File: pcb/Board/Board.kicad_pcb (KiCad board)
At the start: 2 copper layers, 132.1 x 73.3 mm, 69 parts, among them J1 Conn_01x04_Female, J2 TRRS_SJ1-42514, J3 Conn_01x12_Female, K00 KEYSW, K01 KEYSW, K02 KEYSW, K03 KEYSW, K04 KEYSW, K05 KEYSW, K10 KEYSW, K11 KEYSW, K12 KEYSW, K13 KEYSW, K14 KEYSW, K15 KEYSW, K20 KEYSW, K21 KEYSW, K22 KEYSW, K23 KEYSW, K24 KEYSW, K25 KEYSW, K26 KEYSW, K30 KEYSW, K31 KEYSW, K32 KEYSW, K33 KEYSW, K34 KEYSW, K35 KEYSW, K36 KEYSW, U2 PI6ULS5V9511AWEX_I2C_HotSwap, U3 MCP23017_SO

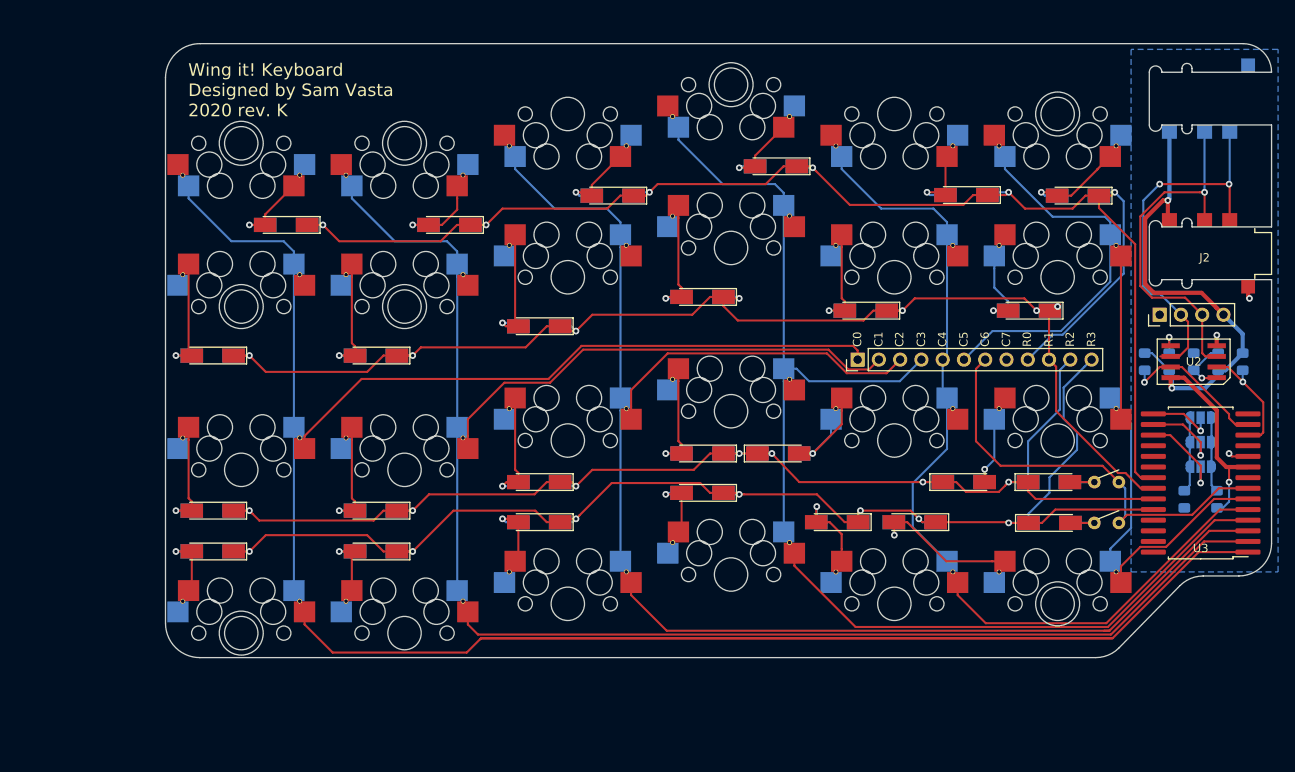
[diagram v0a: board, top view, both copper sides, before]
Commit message: Changed i/o expander to ssop package
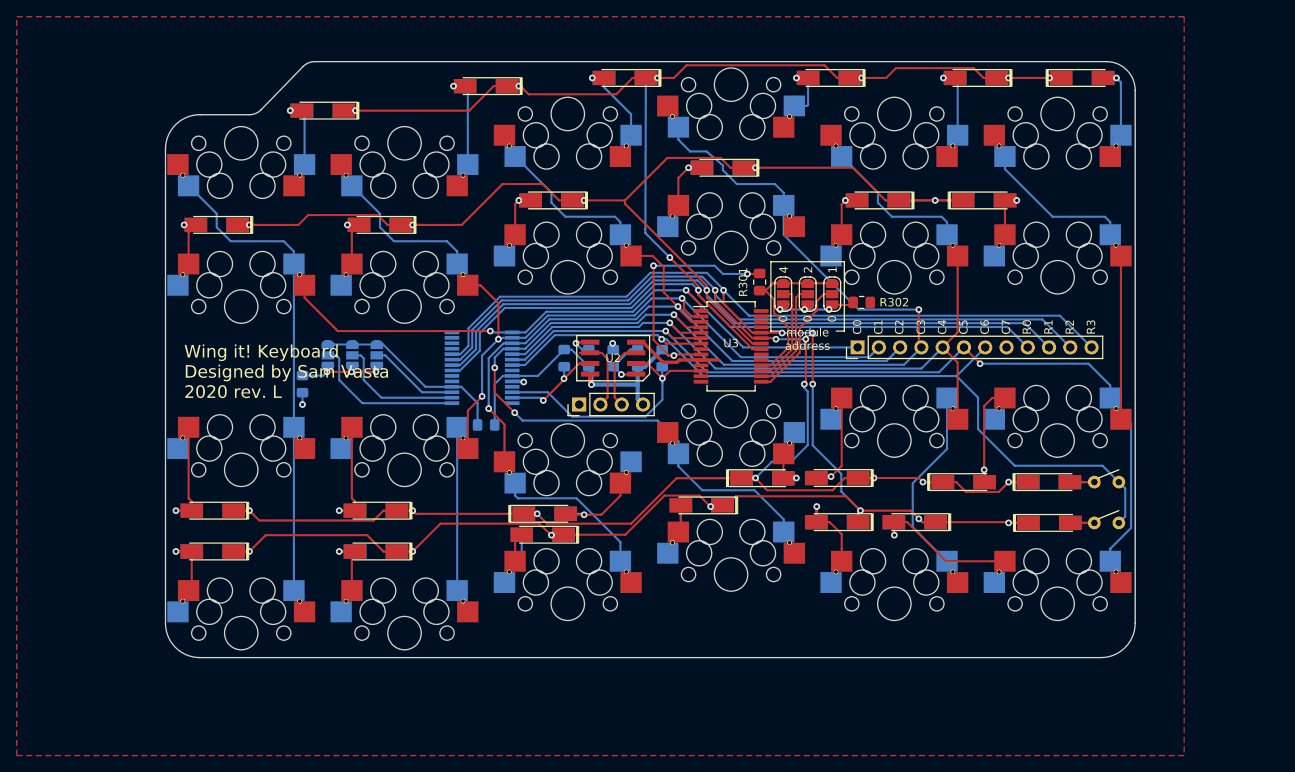
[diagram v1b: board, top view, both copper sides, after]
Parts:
- removed the G*** at (213.3, 48.9)
- removed J2 (x2): TRRS_SJ1-42514, SVastaCustomParts:3.5mm_Cut_out
- removed the U3 at (321.5, 95.3)
- added G***: LOGO, SVastaCustomParts:wing_it_small, B.Cu at (265.4, 111.3)
- added JP0: SolderJumper_3_Open, Jumper:SolderJumper-3_P1.3mm_Open_RoundedPad1.0x1.5mm, F.Cu at (277.5, 72.8)
- added JP1: SolderJumper_3_Open, Jumper:SolderJumper-3_P1.3mm_Open_RoundedPad1.0x1.5mm, F.Cu at (274.6, 72.8)
- added JP2: SolderJumper_3_Open, Jumper:SolderJumper-3_P1.3mm_Open_RoundedPad1.0x1.5mm, F.Cu at (271.6, 72.8)
- added R301: 10K, Resistor_SMD:R_0805_2012Metric_Pad1.15x1.40mm_HandSolder, F.Cu at (268.8, 71.3)
- added R302: 10K, Resistor_SMD:R_0805_2012Metric_Pad1.15x1.40mm_HandSolder, F.Cu at (281.0, 73.8)
- added U3: MCP23017_SO, Package_SO:SSOP-28_5.3x10.2mm_P0.65mm, B.Cu at (235.7, 81.6)
- added U3: MCP23017_SO, Package_SO:SSOP-28_5.3x10.2mm_P0.65mm, F.Cu at (265.4, 79.0)
- moved R302 106.2 mm to (214.2, 83.5)
- moved JP0 104.5 mm to (217.3, 80.1), turned to 270 degrees
- moved JP1 101.8 mm to (220.2, 80.1), turned to 270 degrees
- moved JP2 99.3 mm to (223.1, 80.1), turned to 270 degrees
- moved R301 87.7 mm to (236.2, 88.4), turned to 0 degrees
- moved J1 70.1 mm to (247.3, 86.0)
- moved R201 69.3 mm to (254.3, 80.4)
- moved R203 69.3 mm to (245.5, 80.4)
- moved C201 69.3 mm to (251.3, 80.4)
- moved R202 69.3 mm to (257.2, 80.4)
- moved R204 69.3 mm to (248.4, 80.4)
- moved U2 69.3 mm to (251.3, 80.4)
- moved D01 17.1 mm to (236.2, 47.9)
- moved D13 15.6 mm to (264.4, 57.7)
- moved D10 15.6 mm to (204.0, 64.5)
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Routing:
- net /SwitchMatrix/Col0: track 339.5 -> 147.6 mm, vias 0 -> 2
- net /SwitchMatrix/Col1: track 226.8 -> 128.1 mm, vias 0 -> 3
- net /SwitchMatrix/Row2: track 151.0 -> 232.6 mm, vias 7 -> 11
- net /SwitchMatrix/Row3: track 159.2 -> 240.0 mm, vias 7 -> 11
- net /SwitchMatrix/Row1: track 147.1 -> 215.2 mm, vias 7 -> 6
- net /SwitchMatrix/Col2: track 191.1 -> 130.7 mm, vias 0 -> 2
- net /SwitchMatrix/Col6: track 51.9 -> 98.7 mm, vias 0 -> 1
- net SDA: track 45.8 -> 9.42 mm, vias 2 -> 0
- net Net-(JP0-Pad1): track 8.99 -> 44.5 mm
- net /SwitchMatrix/Row0: track 181.8 -> 217.1 mm, vias 6 -> 8
- net /SwitchMatrix/Col5: track 118.9 -> 154.0 mm, vias 0 -> 2
- net SCL: track 43.0 -> 8.38 mm, vias 1 -> 0
- net Net-(JP0-Pad2): track 7.07 -> 33.9 mm, vias 1 -> 0
- net Net-(JP1-Pad2): track 8.67 -> 28.9 mm, vias 1 -> 0
- net /SwitchMatrix/Col4: track 116.5 -> 134.6 mm, vias 0 -> 1
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- added copper zone on F.Cu, net GND
- removed copper zone on B.Cu, net GND
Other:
- board size 132.1 x 73.3 mm -> 115.8 x 71.2 mm
- rule pad_to_mask_clearance: 0.051 -> 0.05
- board text added: "Wing it! Keyboard Designed by Sam Vasta 2020 rev. L"
- board text removed: "Wing it! Keyboard Designed by Sam Vasta 2020 rev. K"

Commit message: Fixed right-hand i2c connection issue
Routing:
- net SDA_Clean: track 13.6 -> 35.2 mm
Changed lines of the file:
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@@
     (thickness 1.6)
     (drawings 71)
-    (tracks 1029)
+    (tracks 1033)
     (zones 0)
     (modules 73)
@@
   (segment (start 245.461228 82.998995) (end 245.461228 82.873995) (width 0.25) (layer F.Cu) (net 49))
   (segment (start 242.988728 85.471495) (end 245.461228 82.998995) (width 0.25) (layer F.Cu) (net 49))
+  (segment (start 260.688728 82.583995) (end 255.851228 87.421495) (width 0.25) (layer F.Cu) (net 49))
+  (segment (start 261.813728 82.583995) (end 260.688728 82.583995) (width 0.25) (layer F.Cu) (net 49))
+  (segment (start 244.938728 87.421495) (end 242.988728 85.471495) (width 0.25) (layer F.Cu) (net 49))
+  (segment (start 255.851228 87.421495) (end 244.938728 87.421495) (width 0.25) (layer F.Cu) (net 49))
   (via (at 246.888728 78.646495) (size 0.8) (drill 0.4) (layers F.Cu B.Cu) (net 50))
   (segment (start 247.638728 79.396495) (end 246.888728 78.646495) (width 0.25) (layer B.Cu) (net 50))
